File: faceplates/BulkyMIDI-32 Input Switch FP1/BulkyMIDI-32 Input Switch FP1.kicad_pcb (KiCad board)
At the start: 2 copper layers, 100 x 23.2 mm, 5 parts, among them M1 Mounting_Pin, M2 Mounting_Pin, M3 Mounting_Pin, M4 Mounting_Pin

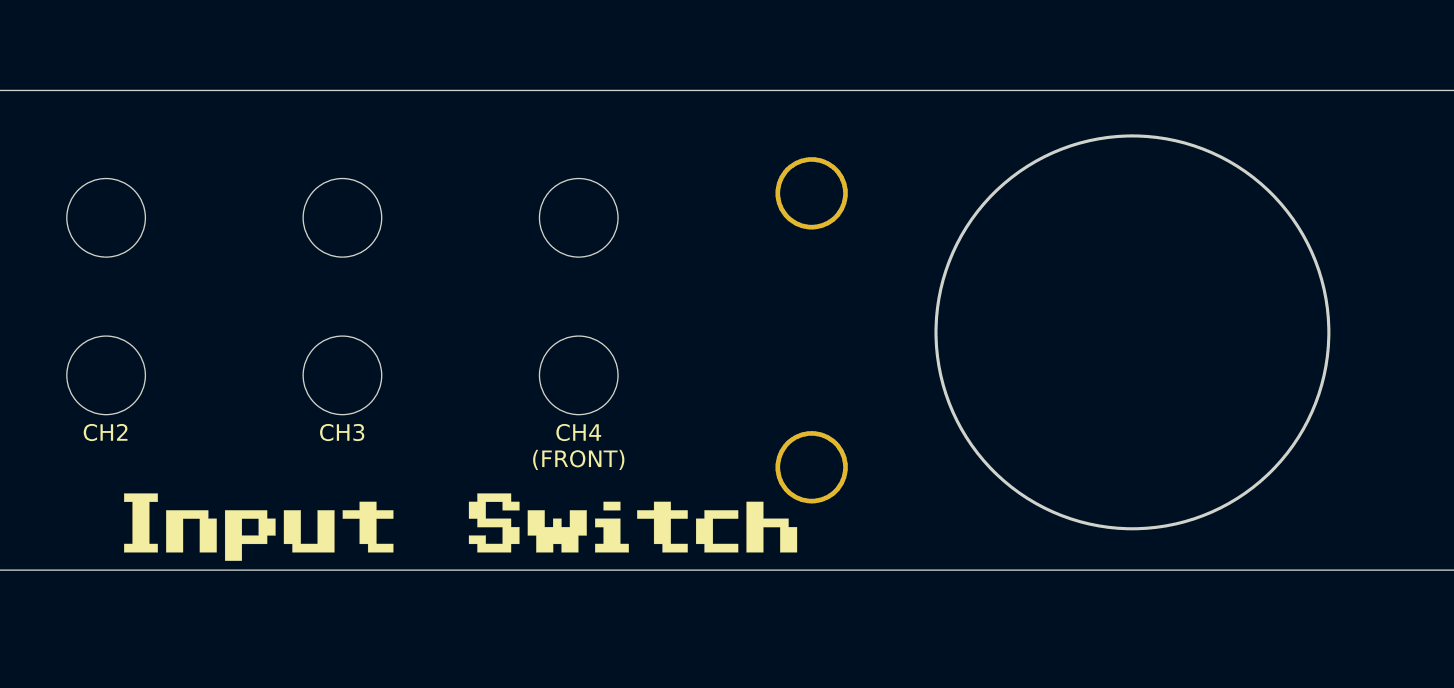
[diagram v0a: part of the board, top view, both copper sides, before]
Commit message: Move cutout up 0.5mm
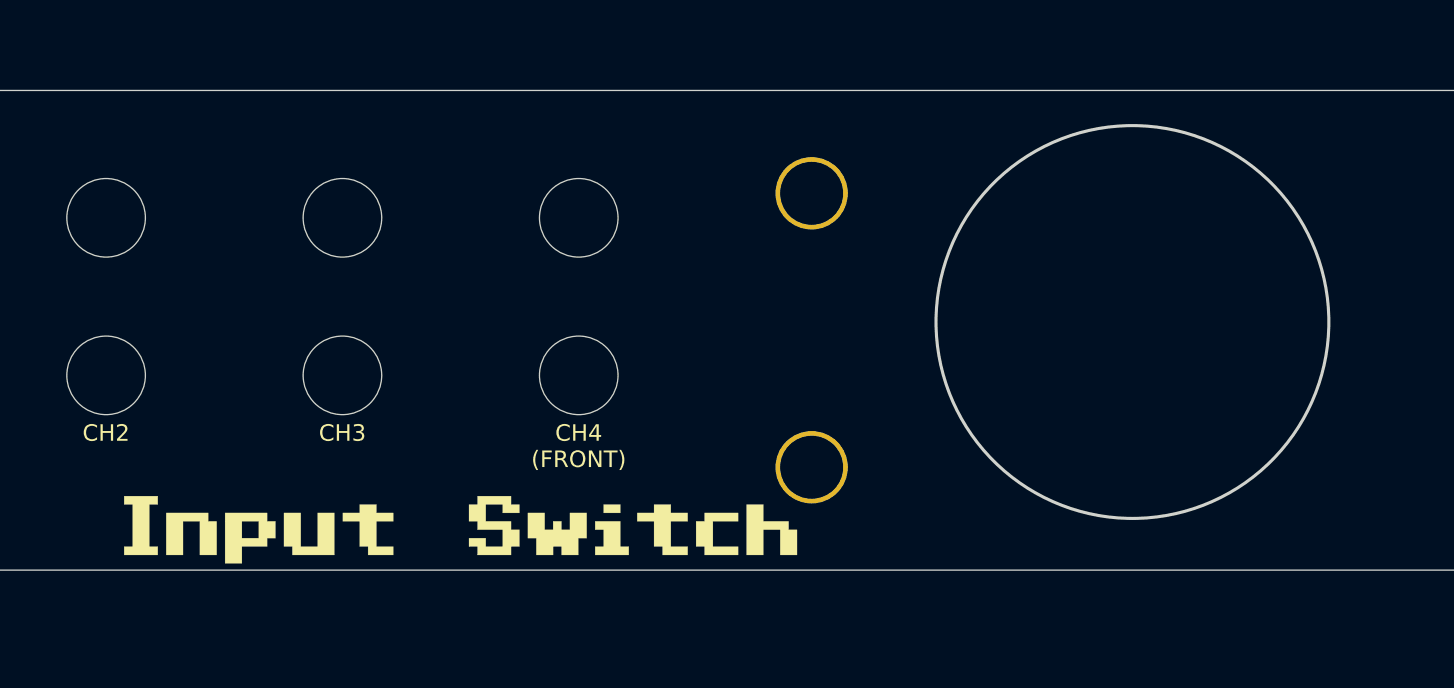
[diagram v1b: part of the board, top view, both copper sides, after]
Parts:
- moved G*** 0.13 mm to (141.1, 132.5)
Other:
- outline, holes or cut-outs redrawn
- board text added: "BulkyMIDI-32 Input Switch FP1 (rev. B) github.com/tebl"
- board text removed: "BulkyMIDI-32 Input Switch FP1 (rev. A) github.com/tebl"

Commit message: Add order number placeholder
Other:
- board text added: "WayWayWay"
